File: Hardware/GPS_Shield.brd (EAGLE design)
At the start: 59.7 x 53.3 mm, 52 parts, among them J1 ARDUINO_R3_SHIELD, J2 USD_CONNECTOR, J3 GP-735-VERTICAL, U1 3.3V, U2 GP3906-TLP, U3 TXB0108

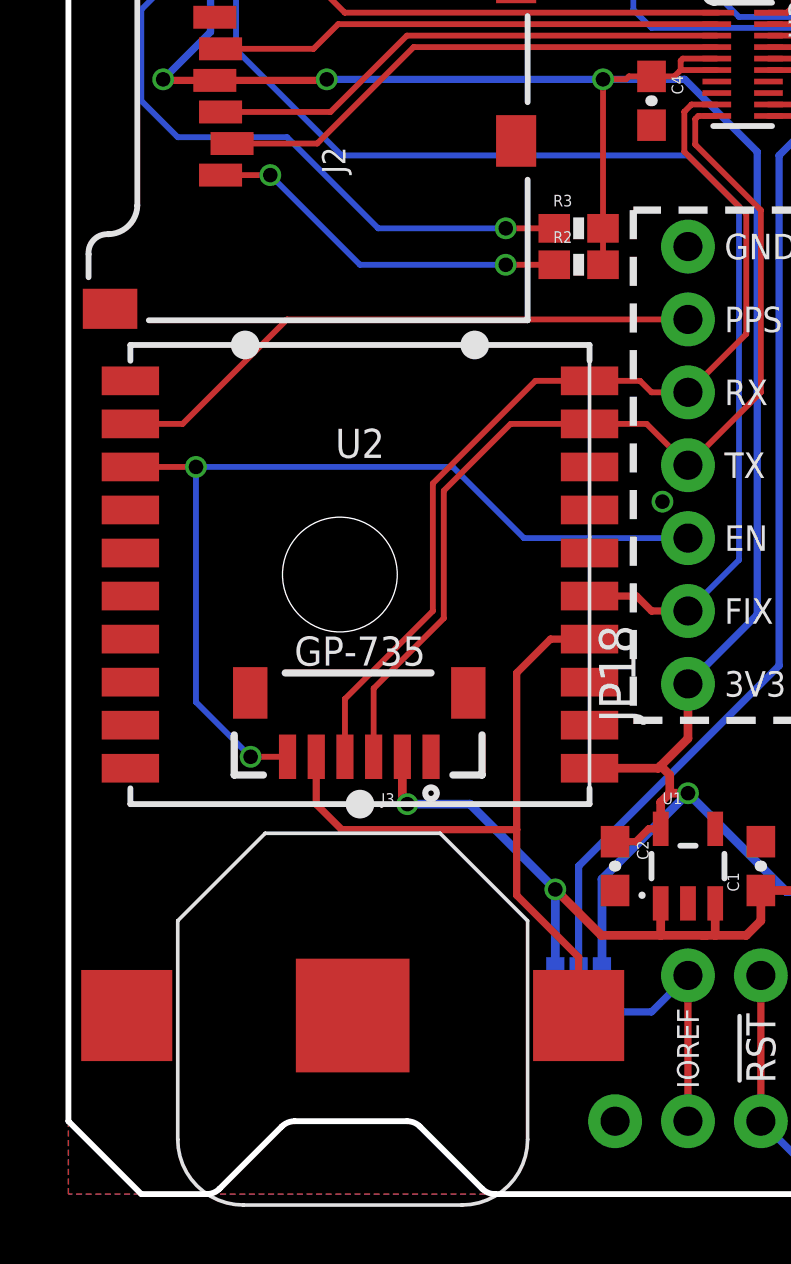
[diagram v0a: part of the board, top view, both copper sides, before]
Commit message: Adding measures, cleaning up schematic
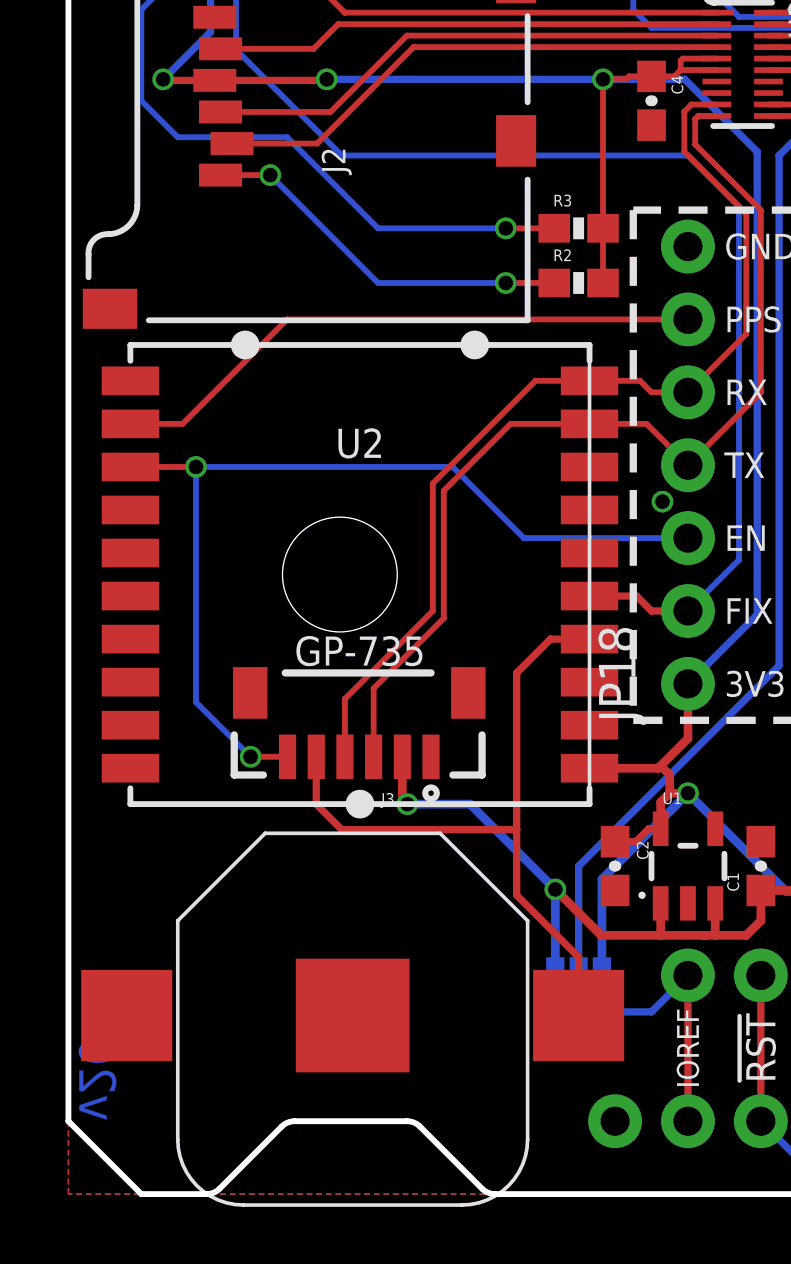
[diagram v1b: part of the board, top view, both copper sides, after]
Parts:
- U1: value 3.3V -> APK2112-3.3V
- moved FRAME1 7.73 mm to (-3.81, -20.3)
- moved R2 0.63 mm to (17.8, 31.8)
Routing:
- net 3.3V: track 116.4 -> 117.1 mm
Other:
- board text added: "Based on a design by Aaron Weiss"
- board text added: "Jim Lindblom"
- board text added: "Units in inches"
- board text added: "v20"
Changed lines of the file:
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@@
 <text x="18.669" y="43.18" size="0.889" layer="21" font="vector" ratio="15" align="center-left">µSD
 CD</text>
+<text x="0.381" y="2.54" size="1.27" layer="16" font="vector" ratio="15" rot="MR90">v20</text>
+<dimension x1="0" y1="0" x2="57.15" y2="0" x3="28.575" y3="-7.62" textsize="1.27" textratio="15" layer="47" dtype="horizontal" unit="inch"/>
+<dimension x1="0" y1="0" x2="59.69" y2="5.08" x3="29.845" y3="-10.16" textsize="1.27" textratio="15" layer="47" dtype="horizontal" unit="inch"/>
+<dimension x1="0" y1="0" x2="2.54" y2="0" x3="1.27" y3="-2.54" textsize="1.27" textratio="15" layer="47" dtype="horizontal" unit="inch"/>
+<dimension x1="0" y1="0" x2="0" y2="2.54" x3="-1.27" y3="1.27" textsize="1.27" textratio="15" layer="47" dtype="vertical" unit="inch"/>
+<dimension x1="0" y1="0" x2="0" y2="50.8" x3="-11.43" y3="25.4" textsize="1.27" textratio="15" layer="47" dtype="vertical" unit="inch"/>
+<dimension x1="0" y1="0" x2="2.54" y2="53.34" x3="-16.51" y3="26.67" textsize="1.27" textratio="15" layer="47" dtype="vertical" unit="inch"/>
+<dimension x1="0" y1="0" x2="59.69" y2="38.1" x3="-6.35" y3="19.05" textsize="1.27" textratio="15" layer="47" dtype="vertical" unit="inch"/>
+<dimension x1="0" y1="0" x2="57.15" y2="40.64" x3="-8.89" y3="20.32" textsize="1.27" textratio="15" layer="47" dtype="vertical" unit="inch"/>
+<dimension x1="0" y1="0" x2="57.15" y2="52.07" x3="-13.97" y3="26.035" textsize="1.27" textratio="15" layer="47" dtype="vertical" unit="inch"/>
+<dimension x1="0" y1="0" x2="59.69" y2="5.08" x3="-3.81" y3="2.54" textsize="1.27" textratio="15" layer="47" dtype="vertical" unit="inch"/>
+<dimension x1="0" y1="0" x2="55.88" y2="53.34" x3="27.94" y3="-5.08" textsize="1.27" textratio="15" layer="47" dtype="horizontal" unit="inch"/>
+<text x="-17.78" y="-6.35" size="1.27" layer="47" font="vector" ratio="15">Units in inches</text>
+<text x="26.67" y="-20.32" size="1.778" layer="51" font="vector" ratio="15">Jim Lindblom</text>
+<text x="7.62" y="-22.86" size="1.778" layer="51" font="vector" ratio="15">Based on a design by Aaron Weiss</text>
 </plain>
 <attributes>
@@
 <element name="JP20" library="SparkFun-Aesthetics" package="FIDUCIAL-1X2" value="FIDUCIAL1X2" x="55.88" y="5.08" rot="R270"/>
 <element name="JP19" library="SparkFun-Aesthetics" package="FIDUCIAL-1X2" value="FIDUCIAL1X2" x="1.27" y="50.165" rot="R270"/>
-<element name="FRAME1" library="SparkFun-Aesthetics" package="CREATIVE_COMMONS" value="FRAME-LETTER" x="-5.08" y="-12.7"/>
+<element name="FRAME1" library="SparkFun-Aesthetics" package="CREATIVE_COMMONS" value="FRAME-LETTER" x="-3.81" y="-20.32"/>
 <element name="JP14" library="SparkFun-Connectors" package="1X10_NO_SILK" value="" x="32.766" y="45.72" rot="R180">
 <attribute name="PROD_ID" value="CONN-11563" x="32.766" y="45.72" size="1.778" layer="27" font="vector" ratio="15" rot="R180" display="off"/>
@@
 <attribute name="PROD_ID" value="RES-00818" x="3.81" y="49.53" size="1.778" layer="27" font="vector" ratio="15" rot="R180" display="off"/>
 </element>
-<element name="U1" library="SparkFun-PowerIC" package="SOT23-5" value="3.3V" x="21.59" y="11.43">
+<element name="U1" library="SparkFun-PowerIC" package="SOT23-5" value="APK2112-3.3V" x="21.59" y="11.43">
 <attribute name="PROD_ID" value="VREG-12457" x="21.59" y="11.43" size="1.778" layer="27" font="vector" ratio="15" display="off"/>
 </element>
@@
 <attribute name="PROD_ID" value="CONN-07820" x="16.002" y="44.45" size="0.889" layer="27" font="vector" ratio="15" rot="R90" display="off"/>
 </element>
-<element name="R2" library="SparkFun-Resistors" package="0603-RES" value="100k" x="17.78" y="32.385">
-<attribute name="PROD_ID" value="RES-07828" x="17.78" y="32.385" size="0.889" layer="27" font="vector" ratio="15" display="off"/>
+<element name="R2" library="SparkFun-Resistors" package="0603-RES" value="100k" x="17.78" y="31.75">
+<attribute name="PROD_ID" value="RES-07828" x="17.78" y="31.75" size="0.889" layer="27" font="vector" ratio="15" display="off"/>
 </element>
 <element name="R3" library="SparkFun-Resistors" package="0603-RES" value="100k" x="17.78" y="33.655">
@@
 <wire x1="5.102" y1="38.81" x2="3.338575" y2="38.81" width="0.254" layer="1"/>
 <wire x1="3.338575" y1="38.81" x2="3.302" y2="38.846575" width="0.254" layer="1"/>
-<wire x1="18.63" y1="32.385" x2="18.63" y2="33.655" width="0.2032" layer="1"/>
+<wire x1="18.63" y1="31.75" x2="18.63" y2="33.655" width="0.2032" layer="1"/>
 <wire x1="18.63" y1="38.846575" x2="18.63" y2="33.655" width="0.2032" layer="1"/>
 </signal>
@@
 <contactref element="R2" pad="1"/>
 <wire x1="5.302" y1="35.51" x2="7.035" y2="35.51" width="0.2032" layer="1"/>
-<wire x1="16.93" y1="32.385" x2="15.24" y2="32.385" width="0.2032" layer="1"/>
+<wire x1="16.93" y1="31.75" x2="15.24" y2="31.75" width="0.2032" layer="1"/>
 <via x="7.035" y="35.51" extent="1-16" drill="0.508"/>
-<wire x1="7.035" y1="35.51" x2="10.16" y2="32.385" width="0.2032" layer="16"/>
-<wire x1="10.16" y1="32.385" x2="15.24" y2="32.385" width="0.2032" layer="16"/>
-<via x="15.24" y="32.385" extent="1-16" drill="0.508"/>
+<wire x1="7.035" y1="35.51" x2="10.795" y2="31.75" width="0.2032" layer="16"/>
+<wire x1="10.795" y1="31.75" x2="15.24" y2="31.75" width="0.2032" layer="16"/>
+<via x="15.24" y="31.75" extent="1-16" drill="0.508"/>
 </signal>
 <signal name="N$19">

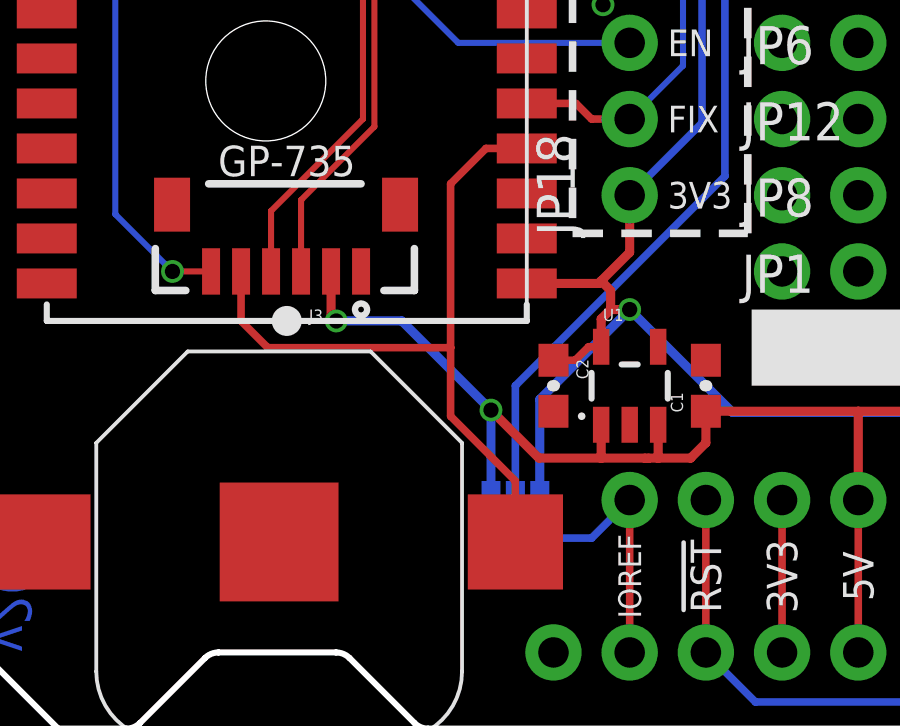
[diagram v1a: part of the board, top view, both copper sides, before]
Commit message: Changing GP-735 module's VCC to 3.3V
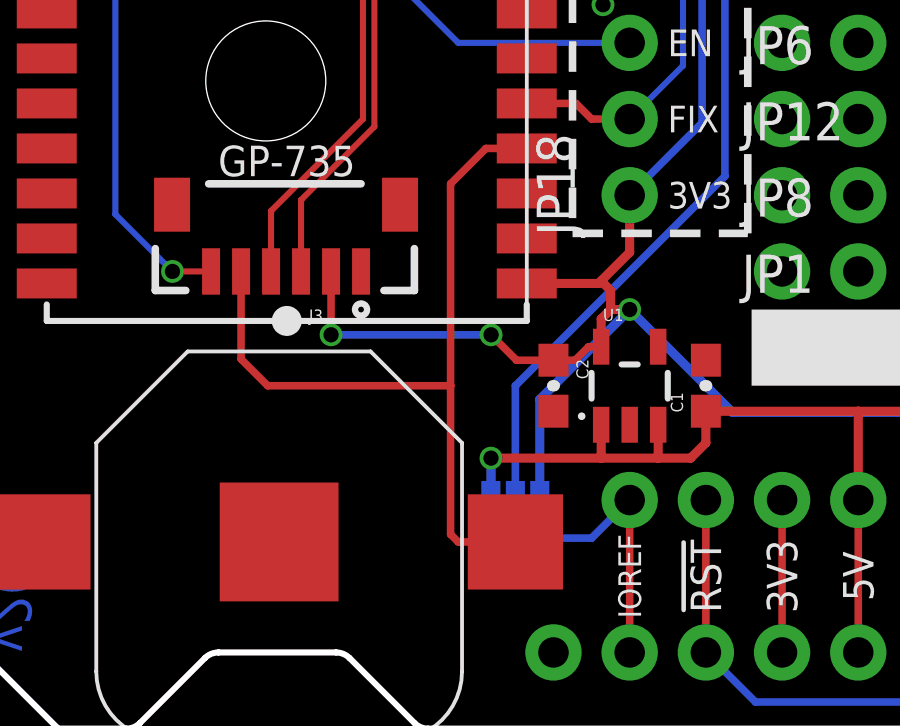
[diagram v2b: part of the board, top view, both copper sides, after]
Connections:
- net 3.3V: now also J3.2
- net 5V: no longer J3.2
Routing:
- net 5V: track 59.3 -> 48.9 mm, vias 2 -> 1
- net 3.3V: track 117.1 -> 127.0 mm, vias 5 -> 7
- net V_BATT: track 24.9 -> 27.2 mm
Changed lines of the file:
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@@
 <layer number="47" name="Measures" color="7" fill="1" visible="no" active="yes"/>
 <layer number="48" name="Document" color="7" fill="1" visible="no" active="yes"/>
-<layer number="49" name="Reference" color="7" fill="1" visible="yes" active="yes"/>
+<layer number="49" name="Reference" color="7" fill="1" visible="no" active="yes"/>
 <layer number="50" name="dxf" color="7" fill="1" visible="no" active="yes"/>
 <layer number="51" name="tDocu" color="6" fill="1" visible="yes" active="yes"/>
@@
 <wire x1="18.63" y1="31.75" x2="18.63" y2="33.655" width="0.2032" layer="1"/>
 <wire x1="18.63" y1="38.846575" x2="18.63" y2="33.655" width="0.2032" layer="1"/>
+<contactref element="J3" pad="2"/>
+<wire x1="11.6365" y1="15.24" x2="11.6365" y2="13.1285" width="0.254" layer="1"/>
+<via x="11.6365" y="13.1285" extent="1-16" drill="0.508"/>
+<wire x1="11.6365" y1="13.1285" x2="16.9705" y2="13.1285" width="0.254" layer="16"/>
+<via x="16.9705" y="13.1285" extent="1-16" drill="0.508"/>
+<wire x1="16.9705" y1="13.1285" x2="17.819" y2="12.28" width="0.254" layer="1"/>
+<wire x1="17.819" y1="12.28" x2="19.05" y2="12.28" width="0.254" layer="1"/>
 </signal>
 <signal name="5V">
-<contactref element="J3" pad="2"/>
 <contactref element="SJ3" pad="3"/>
 <contactref element="U1" pad="1"/>
@@
 <wire x1="52.07" y1="11.303" x2="51.347" y2="10.58" width="0.3048" layer="1"/>
 <wire x1="29.21" y1="7.62" x2="29.21" y2="10.58" width="0.3048" layer="1"/>
-<wire x1="22.098" y1="9.017" x2="20.64" y2="9.017" width="0.3048" layer="1"/>
-<wire x1="20.64" y1="9.017" x2="18.5674" y2="9.017" width="0.3048" layer="1"/>
-<wire x1="16.9672" y1="10.6172" x2="16.9672" y2="7.62" width="0.3048" layer="16"/>
+<wire x1="22.54" y1="9.017" x2="20.64" y2="9.017" width="0.3048" layer="1"/>
+<wire x1="20.64" y1="9.017" x2="16.9672" y2="9.017" width="0.3048" layer="1"/>
 <wire x1="20.64" y1="10.1299" x2="20.64" y2="9.017" width="0.3048" layer="1"/>
-<wire x1="11.6365" y1="15.24" x2="11.6365" y2="13.7635" width="0.3048" layer="1"/>
-<wire x1="11.6365" y1="13.7635" x2="11.811" y2="13.589" width="0.3048" layer="1"/>
-<via x="11.811" y="13.589" extent="1-16" drill="0.508"/>
-<wire x1="11.811" y1="13.589" x2="13.9954" y2="13.589" width="0.3048" layer="16"/>
-<via x="16.9672" y="10.6172" extent="1-16" drill="0.508"/>
-<wire x1="16.9672" y1="10.6172" x2="18.5674" y2="9.017" width="0.3048" layer="1"/>
-<wire x1="16.9672" y1="10.6172" x2="13.9954" y2="13.589" width="0.3048" layer="16"/>
-<wire x1="22.098" y1="9.017" x2="22.225" y2="9.017" width="0.3048" layer="1"/>
 <wire x1="22.54" y1="9.017" x2="23.622" y2="9.017" width="0.3048" layer="1"/>
 <wire x1="23.622" y1="9.017" x2="24.13" y2="9.525" width="0.3048" layer="1"/>
 <wire x1="24.13" y1="9.525" x2="24.13" y2="10.58" width="0.3048" layer="1"/>
 <wire x1="22.54" y1="10.1299" x2="22.54" y2="9.017" width="0.3048" layer="1"/>
-<wire x1="22.54" y1="9.017" x2="22.225" y2="9.017" width="0.3048" layer="1"/>
+<via x="16.9672" y="9.017" extent="1-16" drill="0.508"/>
+<wire x1="16.9672" y1="9.017" x2="16.9672" y2="7.62" width="0.3048" layer="16"/>
 </signal>
 <signal name="PPS">
@@
 <contactref element="J3" pad="5"/>
 <contactref element="U2" pad="4"/>
-<wire x1="15.621" y1="12.7" x2="15.621" y2="10.414" width="0.254" layer="1"/>
-<wire x1="17.78" y1="6.223" x2="17.78" y2="8.255" width="0.254" layer="1"/>
-<wire x1="17.78" y1="8.255" x2="15.621" y2="10.414" width="0.254" layer="1"/>
-<wire x1="8.6365" y1="15.24" x2="8.6365" y2="13.5885" width="0.254" layer="1"/>
-<wire x1="8.6365" y1="13.5885" x2="9.525" y2="12.7" width="0.254" layer="1"/>
-<wire x1="9.525" y1="12.7" x2="15.621" y2="12.7" width="0.254" layer="1"/>
-<wire x1="15.621" y1="12.7" x2="15.621" y2="18.161" width="0.254" layer="1"/>
+<wire x1="8.6365" y1="15.24" x2="8.6365" y2="12.3185" width="0.254" layer="1"/>
+<wire x1="8.6365" y1="12.3185" x2="9.525" y2="11.43" width="0.254" layer="1"/>
+<wire x1="9.525" y1="11.43" x2="15.621" y2="11.43" width="0.254" layer="1"/>
+<wire x1="15.621" y1="11.43" x2="15.621" y2="18.161" width="0.254" layer="1"/>
 <wire x1="18.16" y1="19.34" x2="16.8" y2="19.34" width="0.254" layer="1"/>
 <wire x1="16.8" y1="19.34" x2="15.621" y2="18.161" width="0.254" layer="1"/>
+<wire x1="15.621" y1="11.43" x2="15.621" y2="6.477" width="0.254" layer="1"/>
+<wire x1="15.621" y1="6.477" x2="15.875" y2="6.223" width="0.254" layer="1"/>
+<wire x1="17.78" y1="6.223" x2="15.875" y2="6.223" width="0.254" layer="1"/>
 </signal>
 <signal name="CD">

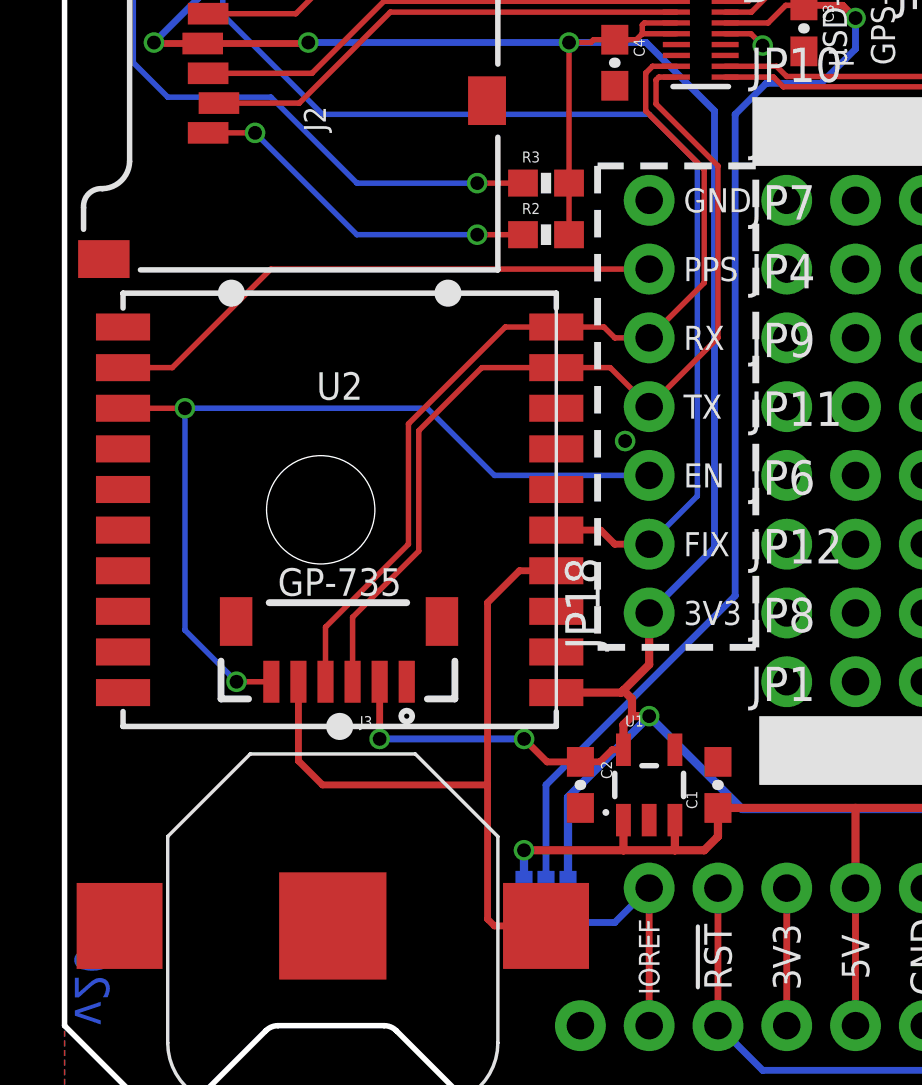
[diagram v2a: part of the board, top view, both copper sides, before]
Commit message: Moving GP-735 connector to bottom side, marking DNP
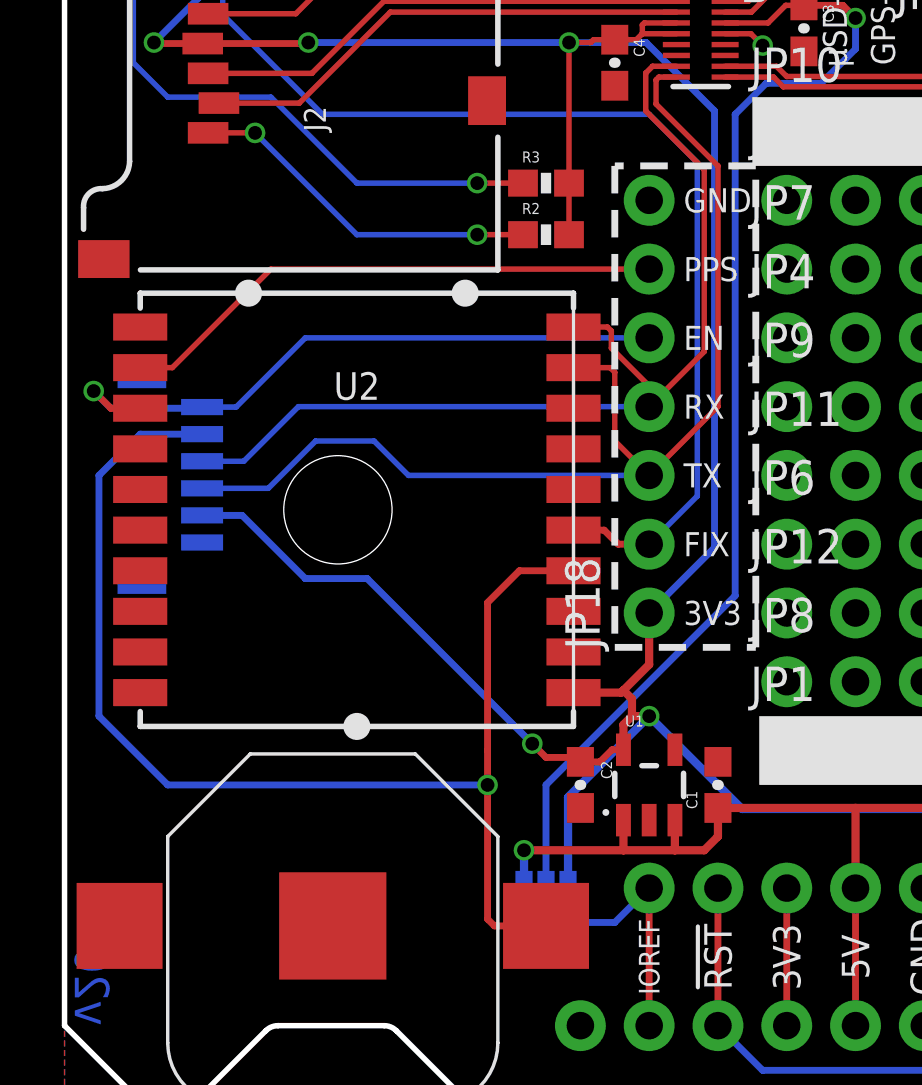
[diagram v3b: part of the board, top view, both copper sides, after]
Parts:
- J3: value GP-735-VERTICAL -> DNP (GP-735-VERTICAL)
- moved J3 9.14 mm to (5.08, 20.4), flipped to the bottom, turned to 90 degrees
- moved U2 0.63 mm to (10.8, 21.6)
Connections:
- net GPS_RST: now also JP18.5; no longer JP18.3
- net GPS_RX: now also JP18.4; no longer JP18.5
- net GPS_TX: now also JP18.3; no longer JP18.4
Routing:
- net V_BATT: track 27.2 -> 46.3 mm, vias 0 -> 1
- net GPS_RST: track 32.6 -> 23.8 mm, vias 2 -> 1
- net 3.3V: track 127.0 -> 134.0 mm, vias 7 -> 6
- net GPS_TX: track 35.2 -> 41.1 mm
- net GPS_RX: track 34.1 -> 37.5 mm
- net GPS_FIX: track 48.7 -> 48.0 mm
- net PPS: track 20.9 -> 20.3 mm
- net GND: vias 2 -> 1
